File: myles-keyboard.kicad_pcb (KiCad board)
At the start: 2 copper layers, 208.8 x 114.3 mm, 52 parts, among them J1 TRRS, J2 OLED, SW00 Key, SW01 Key, SW02 Key, SW03 Key, SW04 Key, SW05 Key, SW10 Key, SW11 Key, SW12 Key, SW13 Key, SW14 Key, SW15 Key, SW16 Key, SW17 Key, SW18 Key, SW20 Key, SW21 Key, SW22 Key, SW23 Key, SW24 Key, SW25 Key, SW26 Key, SW27 Key, SW28 Key, SW30 Key, SW31 Key, SW32 Key, SW33 Key, SW34 Key, SW35 Key, SW36 Key, SW37 Key, SW38 Key, SW40 Key, SW41 Key, SW42 Key, SW43 Key, SW44 Key, SW45 Key, SW46 Key, SW47 Key, SW48 Key, U1 ProMicro

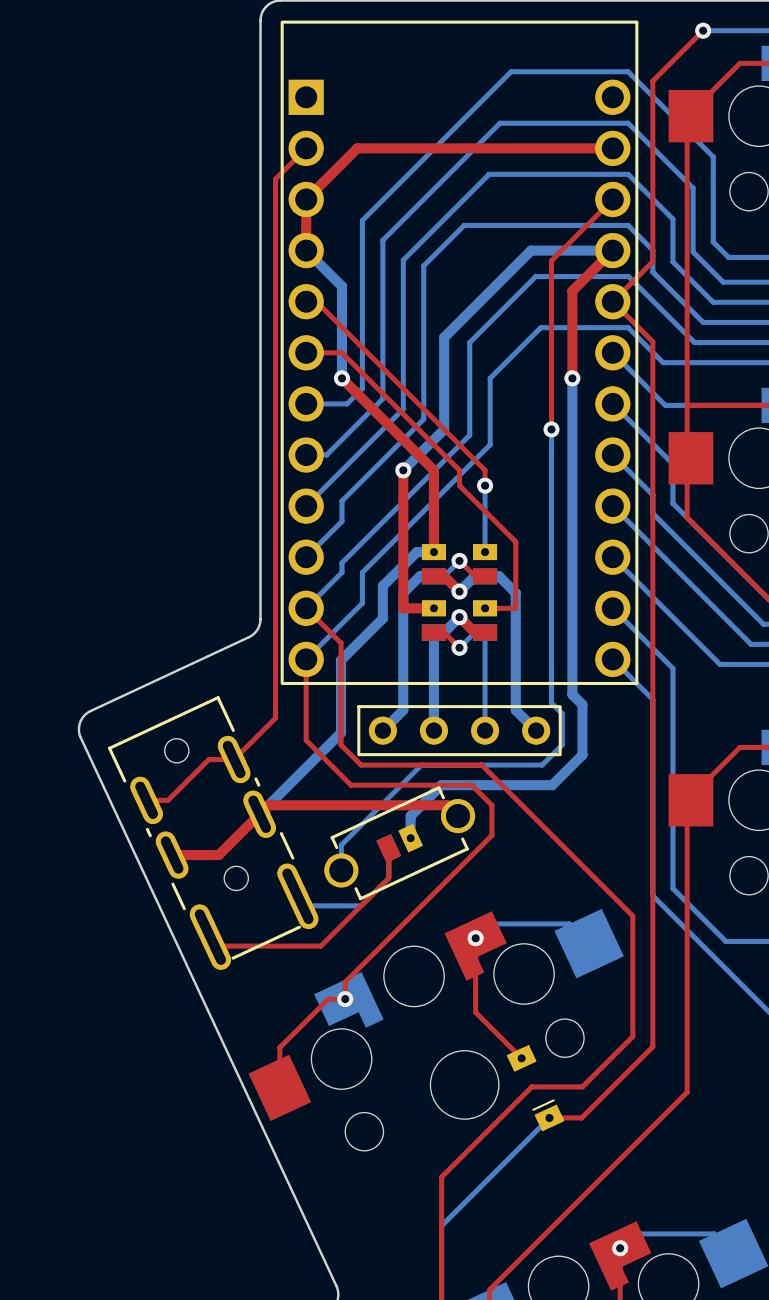
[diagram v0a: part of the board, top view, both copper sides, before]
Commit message: remove OLED
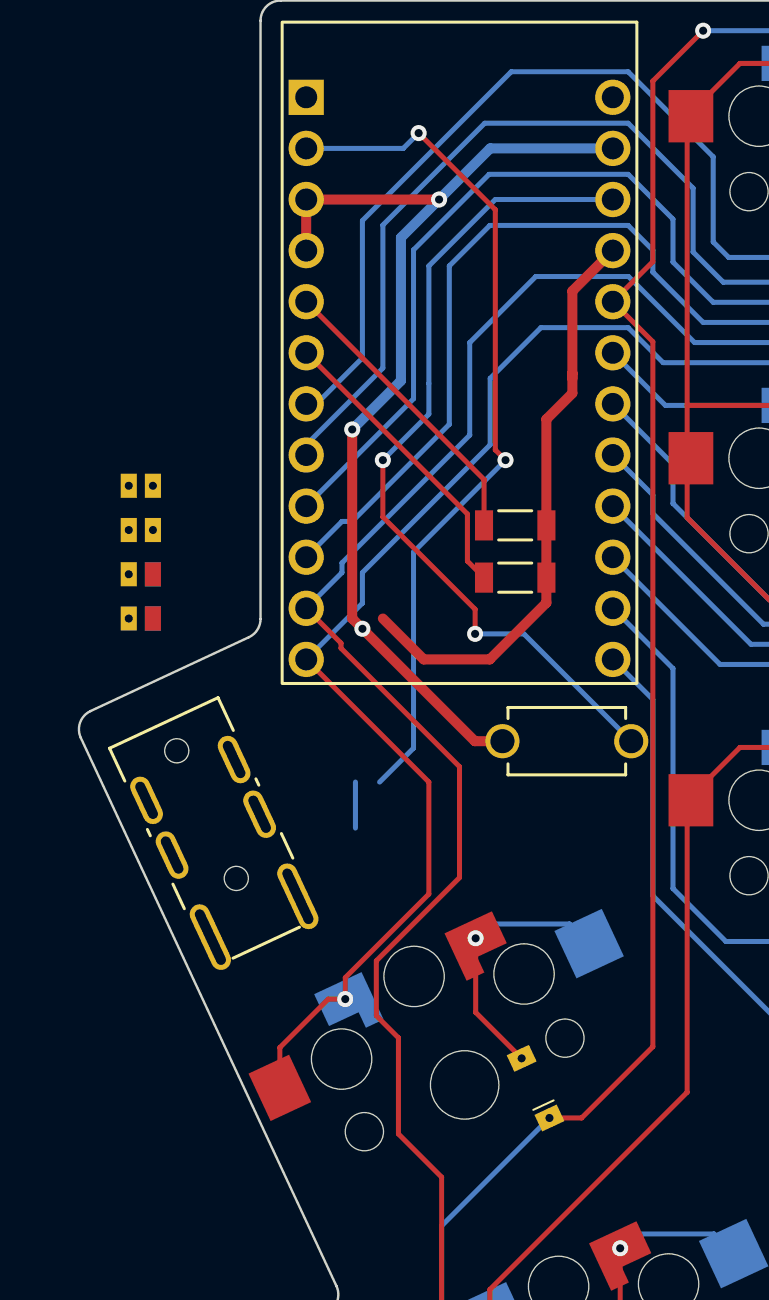
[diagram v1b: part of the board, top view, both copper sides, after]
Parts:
- removed J2: OLED, myles-keyboard:OLED
- removed JP5: ~, myles-keyboard:Jumper
- added R1: R, myles-keyboard:SDR18, F.Cu at (62.7, 76.1)
- added R2: R, myles-keyboard:SDR18, F.Cu at (62.7, 78.7)
- JP1, JP2: value ~ -> JumperSplit
- JP3, JP4: value ~ -> JumperSplit; footprint myles-keyboard:Jumper -> myles-keyboard:JumperSplit
- moved JP1 21.9 mm to (44.0, 74.1), turned to 0 degrees
- moved JP4 17.1 mm to (44.0, 80.7), turned to 0 degrees
- moved JP3 14.7 mm to (44.0, 78.5), turned to 0 degrees
- moved JP2 14.7 mm to (44.0, 76.3), turned to 0 degrees
- moved SW_RST1 9.73 mm to (65.2, 86.8), turned to 180 degrees
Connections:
- J1 pad 1: DATA -> Net-(J1-Pad1)
- J1 pad 6: DATA -> Net-(J1-Pad1)
- JP1 pad 1: VCC -> DATA
- JP1 pad 2: Net-(J1-Pad3) -> Net-(J1-Pad1)
- JP2 pad 1: GND -> SCL
- JP2 pad 2: Net-(J2-Pad4) -> Net-(J1-Pad1)
- JP3 pad 2: Net-(J2-Pad3) -> Net-(J1-Pad3)
- JP3 pad 3: Net-(J2-Pad2) -> Net-(J1-Pad4)
- JP4 pad 1: SCL -> SDA
- JP4 pad 2: Net-(J2-Pad2) -> Net-(J1-Pad4)
- JP4 pad 3: Net-(J2-Pad3) -> Net-(J1-Pad3)
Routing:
- net VCC: track 63.0 -> 29.3 mm, vias 2 -> 0
- net GND: track 69.0 -> 51.4 mm, vias 1 -> 3
- net Net-(J2-Pad4): track 12.3 -> 0.00 mm, vias 1 -> 0
- net Net-(J2-Pad1): track 12.3 -> 0.00 mm, vias 1 -> 0
- net Net-(J1-Pad3): track 11.9 -> 0.00 mm
- net col4: track 269.4 -> 260.0 mm
- net Net-(J2-Pad3): track 8.05 -> 0.00 mm, vias 1 -> 0
- net Net-(J2-Pad2): track 8.05 -> 0.00 mm, vias 1 -> 0
- net col5: track 241.7 -> 235.6 mm
- net DATA: track 37.1 -> 42.5 mm, vias 0 -> 2
- net SCL: track 19.6 -> 14.8 mm
- net Net-(J1-Pad4): track 6.77 -> 2.82 mm
- net SDA: track 16.4 -> 14.8 mm, vias 1 -> 0
- net RESET: track 42.9 -> 41.6 mm, vias 1 -> 2
- net row1: track 216.8 -> 216.0 mm

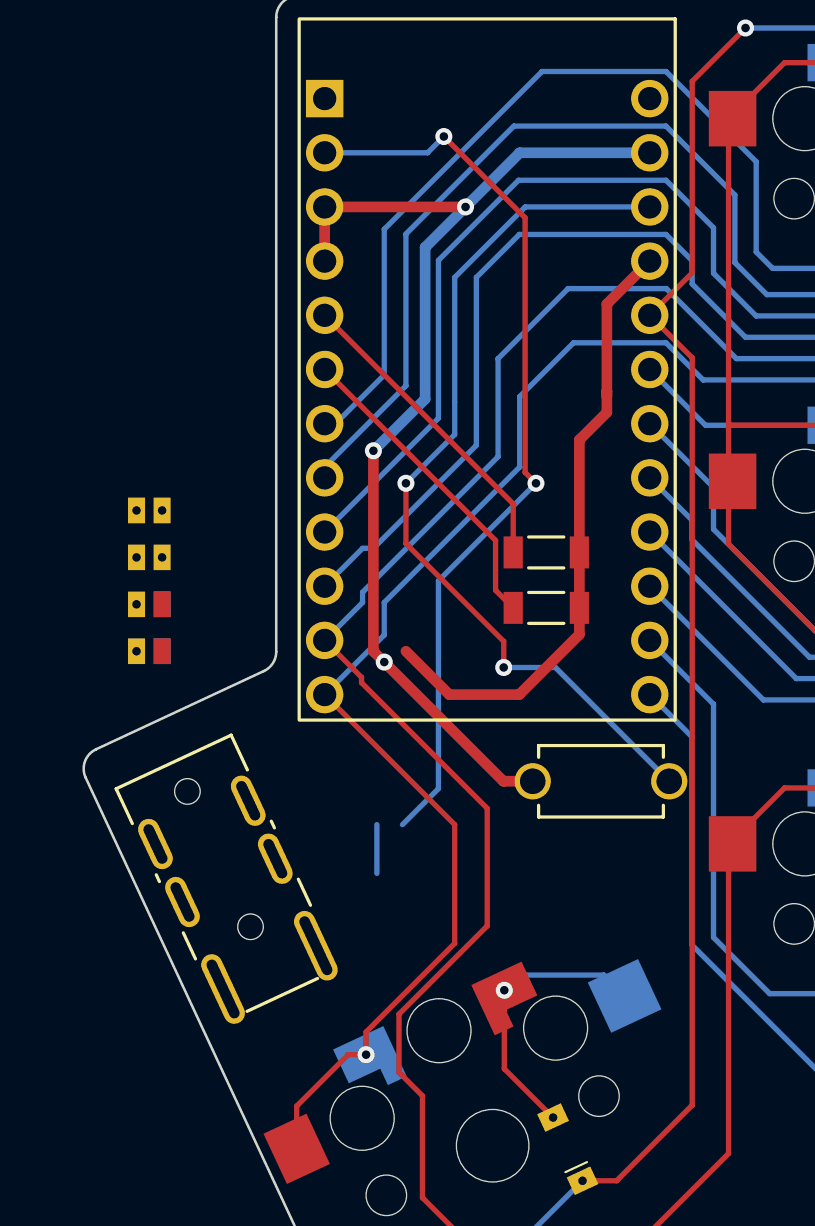
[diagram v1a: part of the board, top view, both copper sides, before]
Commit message: complete draft tracing
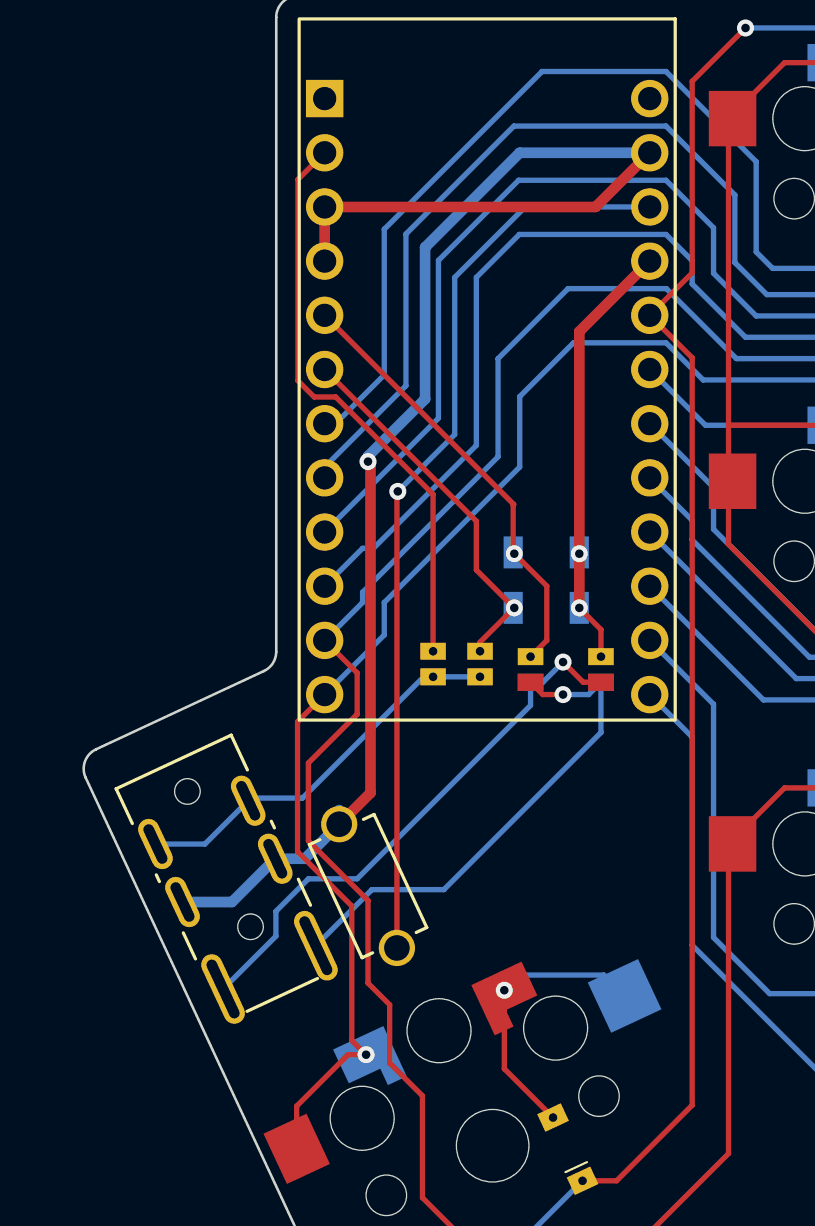
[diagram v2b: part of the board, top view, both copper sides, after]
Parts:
- R1, R2: moved to B.Cu
- moved JP3 21.4 mm to (65.2, 81.6), turned to -90 degrees
- moved JP4 17.9 mm to (61.9, 81.6), turned to -90 degrees
- moved JP2 16.3 mm to (59.6, 81.3), turned to -90 degrees
- moved JP1 15.1 mm to (57.4, 81.3), turned to -90 degrees
- moved SW_RST1 12.0 mm to (54.3, 91.7), turned to 115 degrees
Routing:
- net Net-(J1-Pad3): track 0.00 -> 25.8 mm, vias 0 -> 1
- net Net-(J1-Pad4): track 2.82 -> 23.6 mm, vias 0 -> 1
- net Net-(J1-Pad1): track 0.00 -> 18.5 mm
- net GND: track 51.4 -> 69.5 mm, vias 3 -> 1
- net DATA: track 42.5 -> 27.1 mm, vias 2 -> 0
- net VCC: track 29.3 -> 20.3 mm, vias 0 -> 2
- net SDA: track 14.8 -> 20.7 mm, vias 0 -> 1
- net SCL: track 14.8 -> 17.6 mm, vias 0 -> 1
- net col5: track 235.6 -> 233.2 mm
- net col4: track 260.0 -> 258.4 mm
- net RESET: track 41.6 -> 43.1 mm, vias 2 -> 1

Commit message: adjust pad size for key; reroute with new pads
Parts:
- moved R2 1.27 mm to (63.7, 77.9)
- moved R1 1.03 mm to (63.7, 75.9)
- moved JP2 0.89 mm to (60.1, 82.0)
- moved JP1 0.72 mm to (57.1, 82.0)
- moved JP4 0.49 mm to (62.2, 82.0)
- moved JP3 0.42 mm to (65.2, 82.0)
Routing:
- net col1: track 162.1 -> 153.0 mm
- net SDA: track 20.7 -> 27.5 mm, vias 1 -> 0
- net GND: track 69.5 -> 63.3 mm
- net col4: track 258.4 -> 263.7 mm
- net col2: track 184.4 -> 179.2 mm
- net VCC: track 20.3 -> 25.1 mm, vias 2 -> 0
- net SCL: track 17.6 -> 21.6 mm, vias 1 -> 0
- net col3: track 204.6 -> 201.4 mm
- net row1: track 216.0 -> 213.4 mm
- net col7: track 235.6 -> 233.1 mm
- net DATA: track 27.1 -> 29.5 mm, vias 0 -> 1
- net col6: track 235.3 -> 233.5 mm
- net col0: track 121.4 -> 120.0 mm
- net RESET: track 43.1 -> 41.8 mm
- net col8: track 255.5 -> 254.3 mm
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
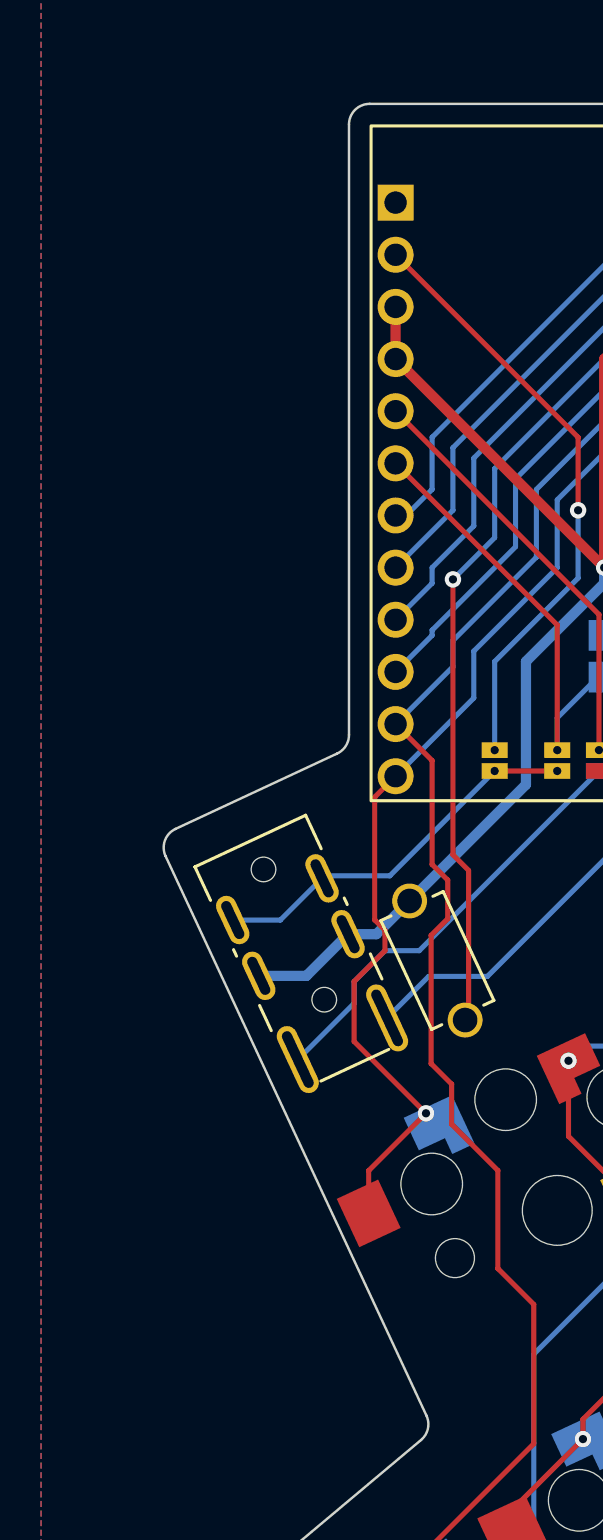
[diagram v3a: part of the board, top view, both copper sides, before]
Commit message: add reset button 3d model and trim 1m off TRRS jack front
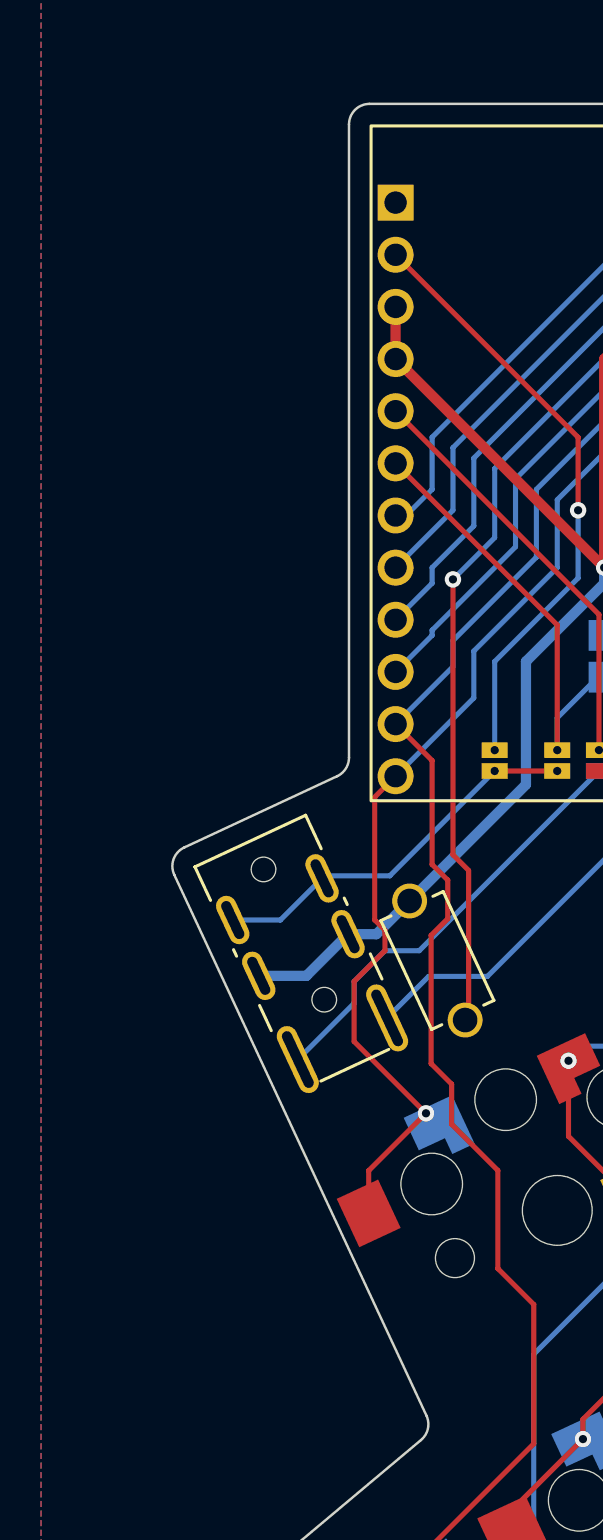
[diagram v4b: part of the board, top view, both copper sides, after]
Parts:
- H1: value ~ -> RightPlate
- moved J1 1.00 mm to (47.7, 91.4)
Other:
- outline, holes or cut-outs redrawn
